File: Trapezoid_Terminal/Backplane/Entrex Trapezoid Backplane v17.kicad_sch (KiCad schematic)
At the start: 18 parts, among them J10 Conn_02x22_Odd_Even, J11 Floppy I/O, J12 Conn_02x15_Odd_Even, J13 Conn_02x15_Odd_Even, J14 Conn_02x15_Odd_Even, J15 Card Edge Connector, J16 Conn_02x50_Odd_Even, J17 trapezoid, J18 Card Edge Connector, J19 trapezoid, J20 trapezoid, J21 Conn_01x07_Pin, J22 Conn_02x12_Odd_Even, J24 Conn_01x08_Pin, J25 Mystery, J9 Conn_02x22_Odd_Even

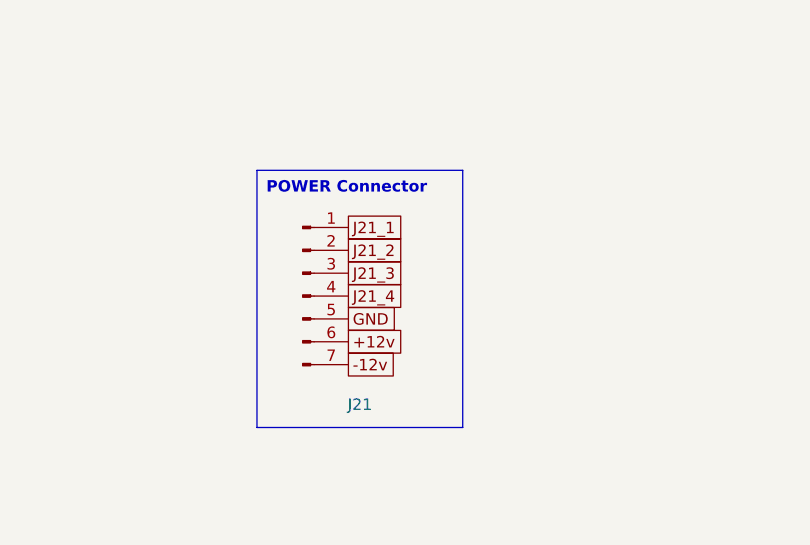
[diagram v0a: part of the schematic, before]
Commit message: Update Backplane PSU Connector
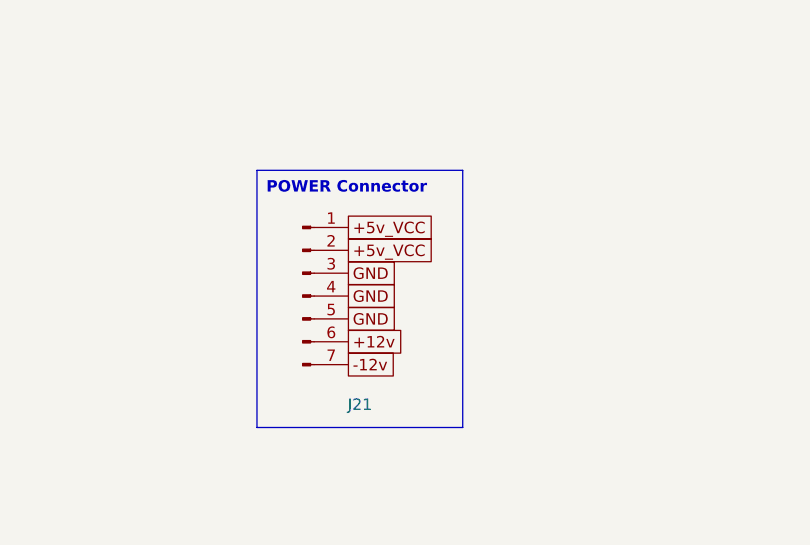
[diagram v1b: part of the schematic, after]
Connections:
- net J21_1 is gone; now on net +5v_VCC: J21.1 (Pin_1)
- net J21_2 is gone; now on net +5v_VCC: J21.2 (Pin_2)
- net J21_3 is gone; now on net GND: J21.3 (Pin_3)
- net J21_4 is gone; now on net GND: J21.4 (Pin_4)
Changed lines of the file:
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@@
     )
   )
-  (global_label "J21_3" (shape passive) (at 945.388 57.15 0) (fields_autoplaced)
+  (global_label "GND" (shape passive) (at 945.388 57.15 0) (fields_autoplaced)
     (effects (font (size 1.27 1.27)) (justify left))
     (property "Intersheetrefs" "${INTERSHEET_REFS}" (at 952.7462 57.15 0)
@@
     )
   )
-  (global_label "J21_1" (shape passive) (at 945.388 52.07 0) (fields_autoplaced)
+  (global_label "+5v_VCC" (shape passive) (at 945.388 52.07 0) (fields_autoplaced)
     (effects (font (size 1.27 1.27)) (justify left))
     (property "Intersheetrefs" "${INTERSHEET_REFS}" (at 952.7462 52.07 0)
@@
     )
   )
-  (global_label "J21_2" (shape passive) (at 945.388 54.61 0) (fields_autoplaced)
+  (global_label "+5v_VCC" (shape passive) (at 945.388 54.61 0) (fields_autoplaced)
     (effects (font (size 1.27 1.27)) (justify left))
     (property "Intersheetrefs" "${INTERSHEET_REFS}" (at 952.7462 54.61 0)
@@
     )
   )
-  (global_label "J21_4" (shape passive) (at 945.388 59.69 0) (fields_autoplaced)
+  (global_label "GND" (shape passive) (at 945.388 59.69 0) (fields_autoplaced)
     (effects (font (size 1.27 1.27)) (justify left))
     (property "Intersheetrefs" "${INTERSHEET_REFS}" (at 952.7462 59.69 0)
